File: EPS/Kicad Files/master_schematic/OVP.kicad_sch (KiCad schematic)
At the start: 6 parts, among them Q1 FZT688BTA, Q2 FZT688BTA

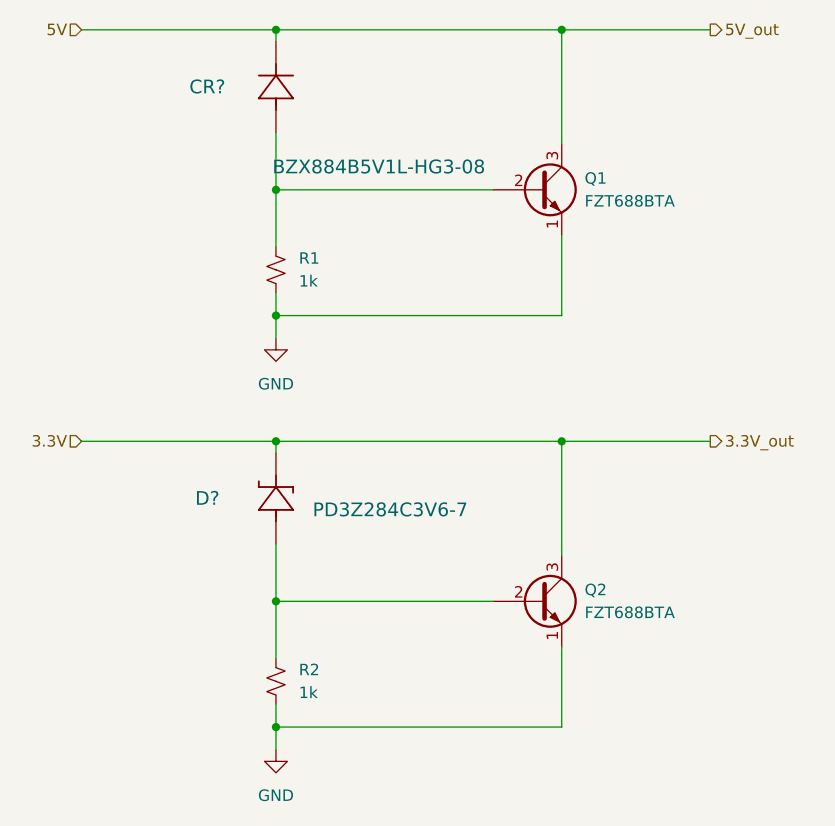
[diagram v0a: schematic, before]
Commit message: updated master schematic
should be nearing final schematic revision. run electrical rules check next
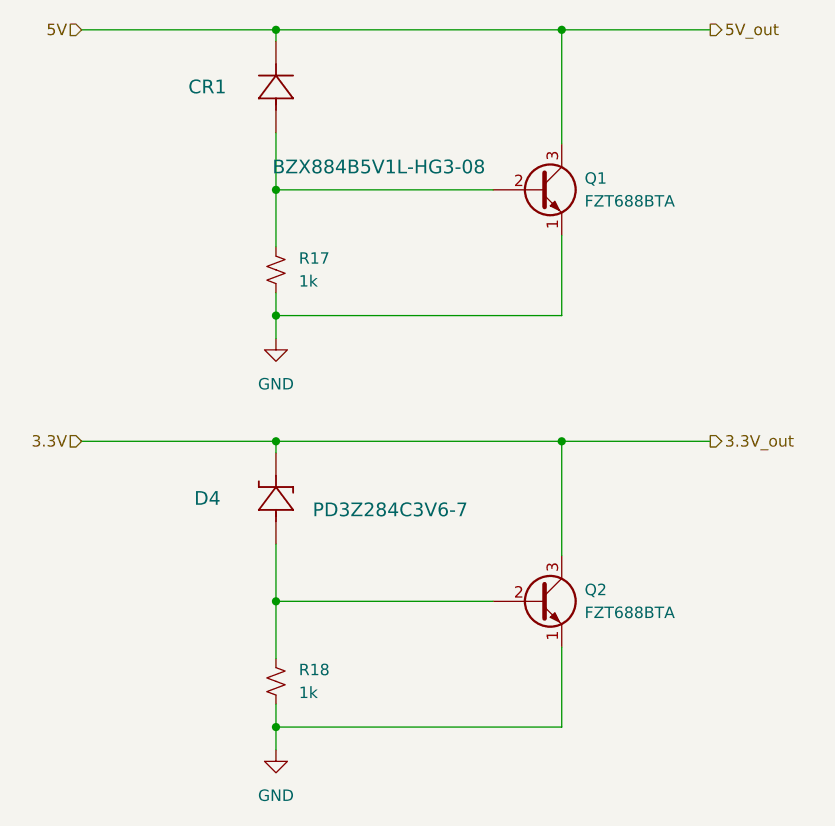
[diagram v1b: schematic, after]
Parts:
- R17: renamed from R1; footprint (none) -> Resistor_SMD:R_0603_1608Metric
- R18: renamed from R2; footprint (none) -> Resistor_SMD:R_0603_1608Metric
- gave numbers to parts that had none: 2
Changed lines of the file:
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@@
   (symbol (lib_id "2022-03-01_22-21-45:BZX884B5V1L-HG3-08") (at 82.55 52.07 90) (unit 1)
     (in_bom yes) (on_board yes)
-    (property "Reference" "CR?" (id 0) (at 74.93 46.99 90)
+    (property "Reference" "CR1" (id 0) (at 74.93 46.99 90)
       (effects (font (size 1.524 1.524)))
     )
@@
   (symbol (lib_id "power:GND") (at 82.55 120.65 0) (unit 1)
     (in_bom yes) (on_board yes) (fields_autoplaced)
-    (property "Reference" "#PWR?" (id 0) (at 82.55 127 0)
+    (property "Reference" "#PWR029" (id 0) (at 82.55 127 0)
       (effects (font (size 1.27 1.27)) hide)
     )
@@
   (symbol (lib_id "Device:R_Small_US") (at 82.55 113.03 0) (unit 1)
     (in_bom yes) (on_board yes) (fields_autoplaced)
-    (property "Reference" "R2" (id 0) (at 85.09 111.7599 0)
+    (property "Reference" "R18" (id 0) (at 85.09 111.7599 0)
       (effects (font (size 1.27 1.27)) (justify left))
     )
@@
       (effects (font (size 1.27 1.27)) (justify left))
     )
-    (property "Footprint" "" (id 2) (at 82.55 113.03 0)
+    (property "Footprint" "Resistor_SMD:R_0603_1608Metric" (id 2) (at 82.55 113.03 0)
       (effects (font (size 1.27 1.27)) hide)
     )
@@
   (symbol (lib_id "2022-03-01_22-23-00:PD3Z284C3V6-7") (at 82.55 97.79 90) (unit 1)
     (in_bom yes) (on_board yes)
-    (property "Reference" "D?" (id 0) (at 74.93 92.71 90)
+    (property "Reference" "D4" (id 0) (at 74.93 92.71 90)
       (effects (font (size 1.524 1.524)))
     )
@@
   (symbol (lib_id "power:GND") (at 82.55 74.93 0) (unit 1)
     (in_bom yes) (on_board yes) (fields_autoplaced)
-    (property "Reference" "#PWR?" (id 0) (at 82.55 81.28 0)
+    (property "Reference" "#PWR028" (id 0) (at 82.55 81.28 0)
       (effects (font (size 1.27 1.27)) hide)
     )
@@
   (symbol (lib_id "Device:R_Small_US") (at 82.55 67.31 0) (unit 1)
     (in_bom yes) (on_board yes) (fields_autoplaced)
-    (property "Reference" "R1" (id 0) (at 85.09 66.0399 0)
+    (property "Reference" "R17" (id 0) (at 85.09 66.0399 0)
       (effects (font (size 1.27 1.27)) (justify left))
     )
@@
       (effects (font (size 1.27 1.27)) (justify left))
     )
-    (property "Footprint" "" (id 2) (at 82.55 67.31 0)
+    (property "Footprint" "Resistor_SMD:R_0603_1608Metric" (id 2) (at 82.55 67.31 0)
       (effects (font (size 1.27 1.27)) hide)
     )

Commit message: EPS master netlist complete
dropped all parts onto pcb
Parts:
- CR1: footprint CR_1L-HG3-08_VIS -> hg3-08:BZX884B5V1L-HG3-08
- D4: footprint PowerDI323_DIO -> PD3z284:PD3Z284C3V6-7
- Q1, Q2: footprint Package_TO_SOT_THT:TO-39-3 -> fzt:SOT230P700X180-4N
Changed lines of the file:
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@@
       (effects (font (size 1.524 1.524)))
     )
-    (property "Footprint" "CR_1L-HG3-08_VIS" (id 2) (at 91.694 46.99 0)
+    (property "Footprint" "hg3-08:BZX884B5V1L-HG3-08" (id 2) (at 91.694 46.99 0)
       (effects (font (size 1.524 1.524)) hide)
     )
@@
       (effects (font (size 1.524 1.524)))
     )
-    (property "Footprint" "PowerDI323_DIO" (id 2) (at 91.694 92.71 0)
+    (property "Footprint" "PD3z284:PD3Z284C3V6-7" (id 2) (at 91.694 92.71 0)
       (effects (font (size 1.524 1.524)) hide)
     )
@@
       (effects (font (size 1.27 1.27)) (justify left))
     )
-    (property "Footprint" "Package_TO_SOT_THT:TO-39-3" (id 2) (at 116.84 60.325 0)
+    (property "Footprint" "fzt:SOT230P700X180-4N" (id 2) (at 116.84 60.325 0)
       (effects (font (size 1.27 1.27) italic) (justify left) hide)
     )
@@
       (effects (font (size 1.27 1.27)) (justify left))
     )
-    (property "Footprint" "Package_TO_SOT_THT:TO-39-3" (id 2) (at 116.84 106.045 0)
+    (property "Footprint" "fzt:SOT230P700X180-4N" (id 2) (at 116.84 106.045 0)
       (effects (font (size 1.27 1.27) italic) (justify left) hide)
     )

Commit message: pcb update
progress on pcb layout
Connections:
- net 3.3V: now also Q2.4 (C); no longer Q2.3 (C)
- net 5V: now also Q1.4 (C); no longer Q1.3 (C)
- net GND: now also Q1.3 (E), Q2.3 (E); no longer Q1.1 (E), Q2.1 (E)
- net at CR1.2, R17.1: now also Q1.1 (B); no longer Q1.2 (B)
- net at D4.2, R18.1: now also Q2.1 (B); no longer Q2.2 (B)
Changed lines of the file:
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@@
     (pin "1")
   )
-  (symbol (lib_id "Transistor_BJT:2N2219") (at 111.76 58.42 0) (unit 1)
+  (symbol (lib_name "2N2219_1") (lib_id "Transistor_BJT:2N2219") (at 111.76 58.42 0) (unit 1)
     (in_bom yes) (on_board yes) (fields_autoplaced)
     (property "Reference" "Q1" (id 0) (at 116.84 57.1499 0)
@@
     )
     (pin "1")
-    (pin "2")
     (pin "3")
+    (pin "4")
   )
   (symbol (lib_id "Device:R_Small_US") (at 82.55 67.31 0) (unit 1)
@@
       (effects (font (size 1.27 1.27)) (justify left) hide)
     )
+    (pin "3")
     (pin "1")
-    (pin "2")
-    (pin "3")
+    (pin "4")
   )
 )

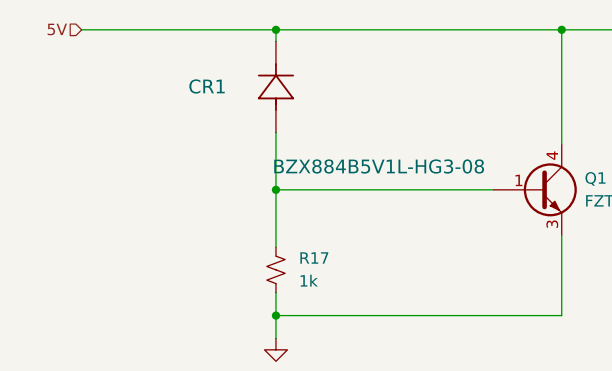
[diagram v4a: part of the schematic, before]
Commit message: eps pcb update
all errors and warnings corrected
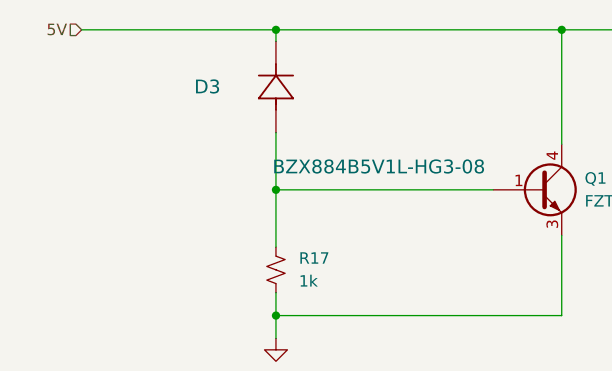
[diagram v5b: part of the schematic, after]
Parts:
- renumbered CR1 to D3
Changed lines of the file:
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@@
   (symbol (lib_id "2022-03-01_22-21-45:BZX884B5V1L-HG3-08") (at 82.55 52.07 90) (unit 1)
     (in_bom yes) (on_board yes)
-    (property "Reference" "CR1" (id 0) (at 74.93 46.99 90)
+    (property "Reference" "D3" (id 0) (at 74.93 46.99 90)
       (effects (font (size 1.524 1.524)))
     )
